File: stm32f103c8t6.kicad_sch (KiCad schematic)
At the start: 0 parts

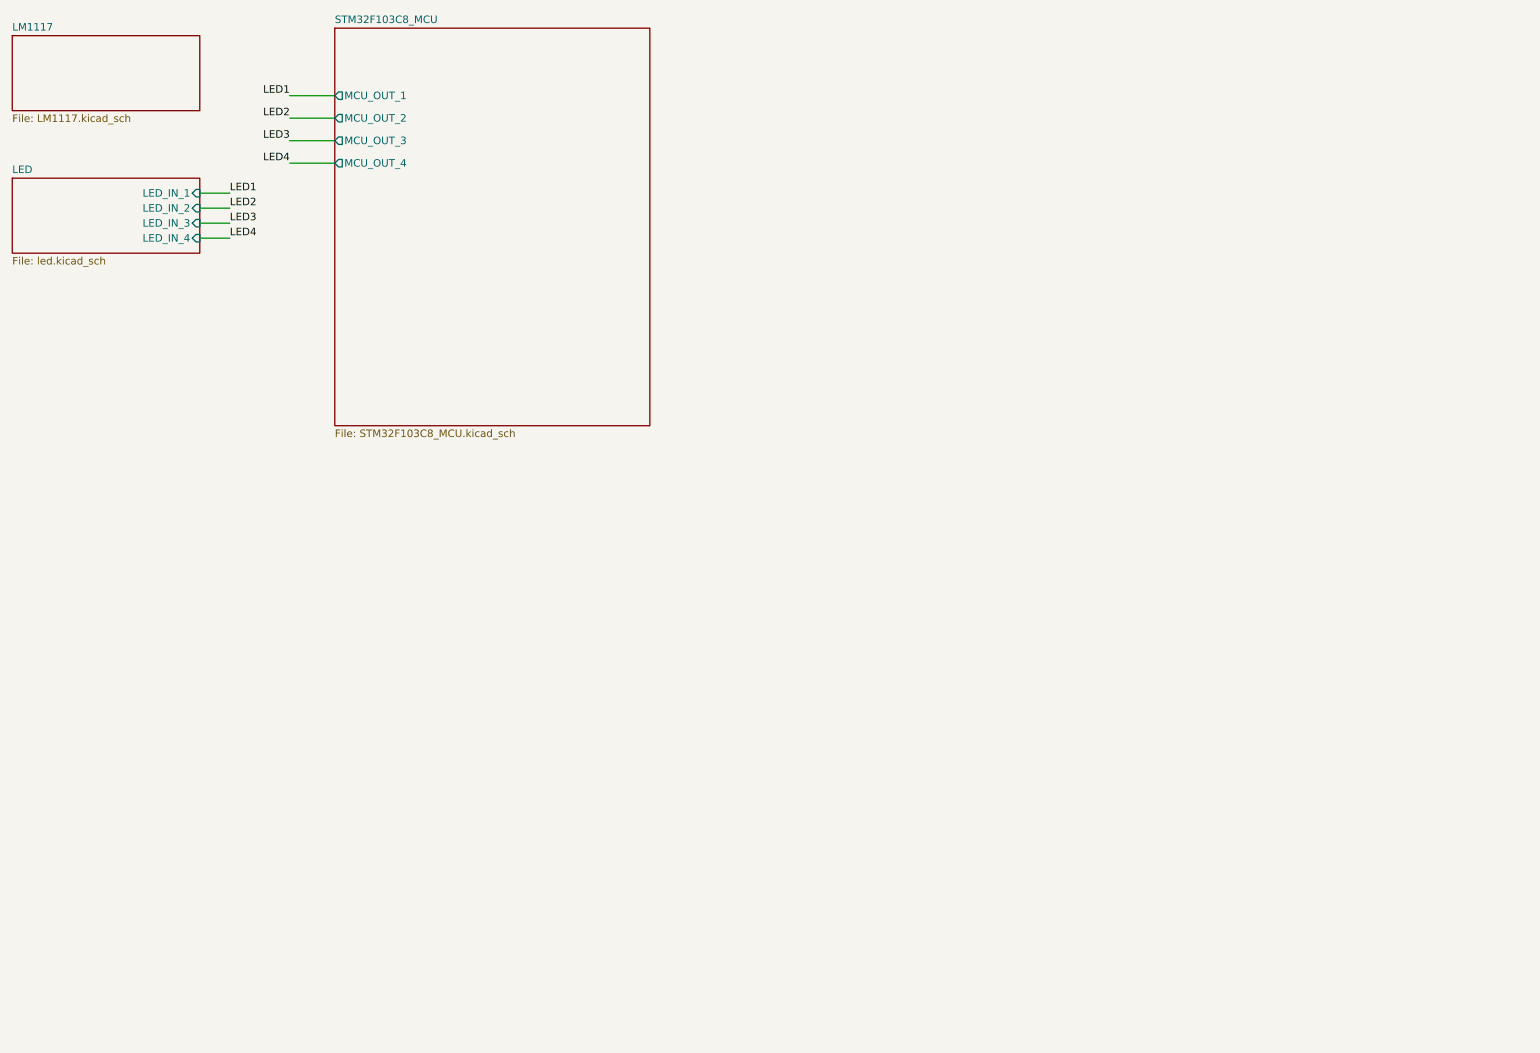
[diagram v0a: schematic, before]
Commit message: Update USB-C and FTDI circuits and add button and potentiometer sheets
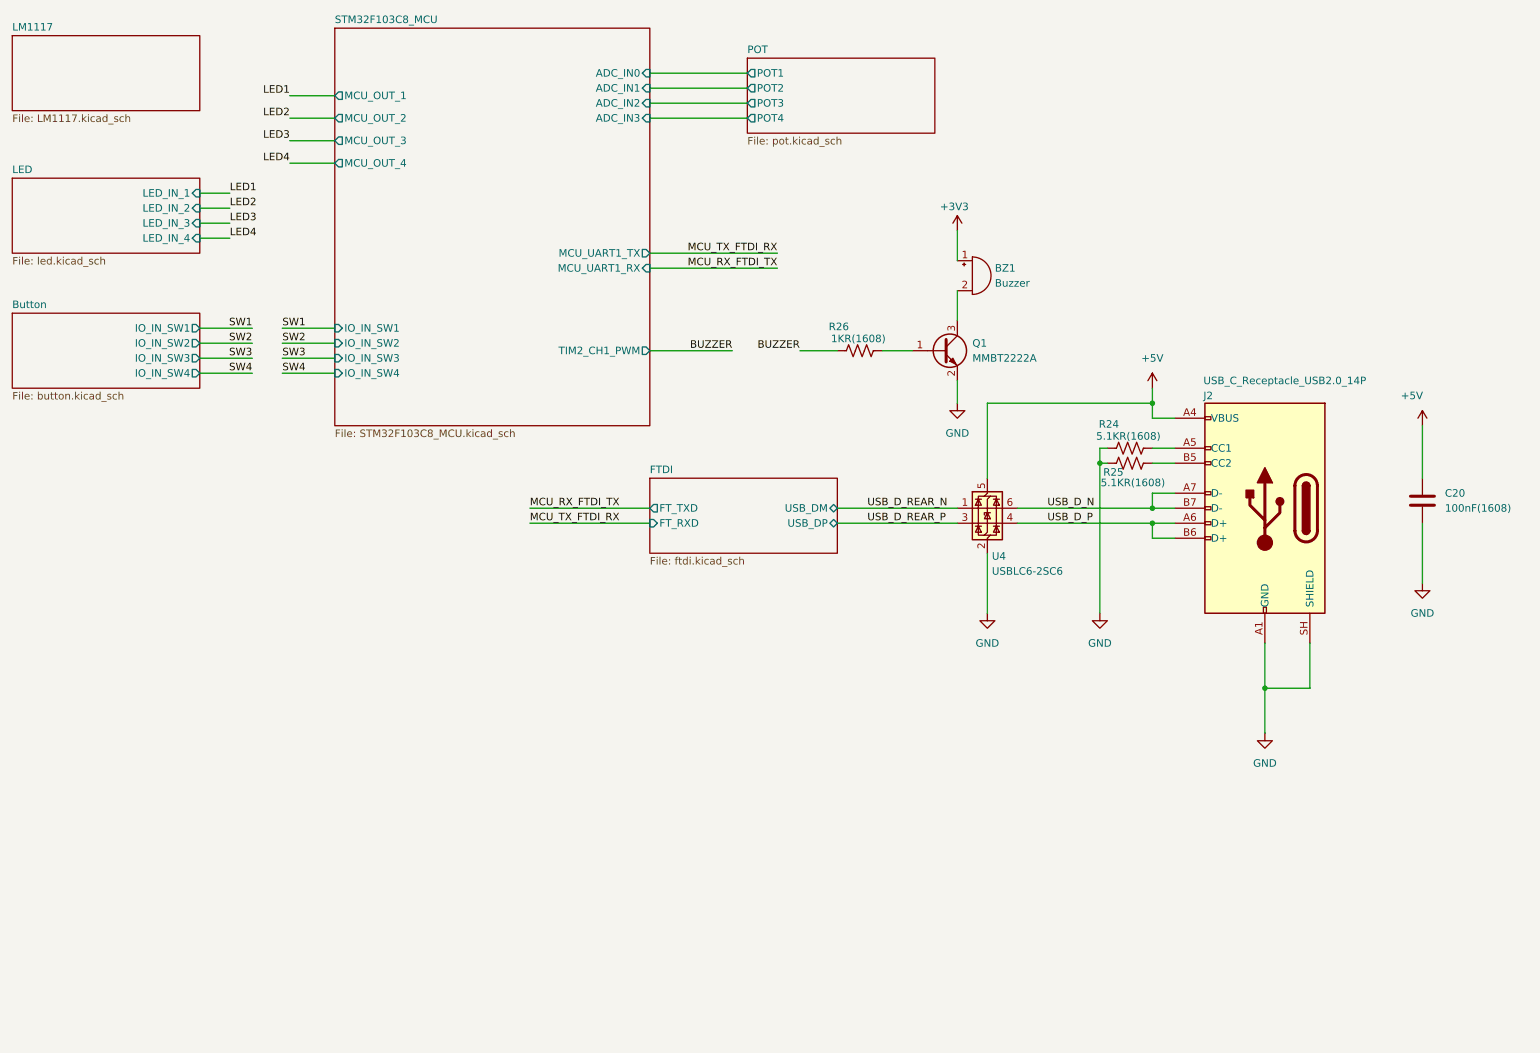
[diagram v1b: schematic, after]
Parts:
- added BZ1: Buzzer, Package_DFN_QFN:Texas_RVA_VQFN-16-1EP_3.5x3.5mm_P0.5mm_EP2.14x2.14mm_ThermalVias, symbol Device:Buzzer
- added C20: 100nF(1608), Capacitor_SMD:C_0603_1608Metric, symbol Device:C
- added J2: USB_C_Receptacle_USB2.0_14P, symbol Connector:USB_C_Receptacle_USB2.0_14P
- added Q1: MMBT2222A, Package_TO_SOT_SMD:SOT-23, symbol Transistor_BJT:MMBT2222A
- added R24, R25: 5.1KR(1608), symbol Device:R_US
- added R26: 1KR(1608), symbol Device:R_US
- added U4: USBLC6-2SC6, Package_TO_SOT_SMD:SOT-23-6, symbol Power_Protection:USBLC6-2SC6
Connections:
- new net: Q1.1 (B), R26.2
- new net: J2.A5 (CC1), R24.2
- new net: BZ1.2 (-), Q1.3 (C)
- new net: J2.B5 (CC2), R25.2
- new net +3V3: BZ1.1 (+)
- new net +5V: C20.1, J2.A4 (VBUS), J2.A9 (VBUS), J2.B4 (VBUS), J2.B9 (VBUS), U4.5 (VBUS)
- new net BUZZER: R26.1
- new net GND: C20.2, J2.A1 (GND), J2.A12 (GND), J2.B1 (GND), J2.B12 (GND), J2.SH (SHIELD), Q1.2 (E), R24.1, R25.1, U4.2 (GND)
- new net USB_D_N: J2.A7 (D-), J2.B7 (D-), U4.6 (I/O1)
- new net USB_D_P: J2.A6 (D+), J2.B6 (D+), U4.4 (I/O2)
- new net USB_D_REAR_N: U4.1 (I/O1)
- new net USB_D_REAR_P: U4.3 (I/O2)
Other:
- added sheet Button (button.kicad_sch)
- added sheet FTDI (ftdi.kicad_sch)
- added sheet POT (pot.kicad_sch)
- sheet STM32F103C8_MCU ports: added ADC_IN0, ADC_IN1, ADC_IN2, ADC_IN3, IO_IN_SW1, IO_IN_SW2, IO_IN_SW3, IO_IN_SW4, MCU_UART1_RX, MCU_UART1_TX, TIM2_CH1_PWM; removed none

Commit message: Update schematics, power flags and PCB design
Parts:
- added H1, H2, H3, H4: MountingHole_Pad, MountingHole:MountingHole_3.2mm_M3_DIN965_Pad, symbol Mechanical:MountingHole_Pad
- added J1: Conn_01x04, Connector_PinHeader_2.54mm:PinHeader_1x04_P2.54mm_Vertical, symbol Connector_Generic:Conn_01x04
- added R1, R2, R3, R4: 0R(1608), Resistor_SMD:R_0603_1608Metric, symbol Device:R_US
- BZ1: footprint Package_DFN_QFN:Texas_RVA_VQFN-16-1EP_3.5x3.5mm_P0.5mm_EP2.14x2.14mm_ThermalVias -> (none)
- R5: renamed from R26; footprint (none) -> Resistor_SMD:R_0603_1608Metric
- R6: renamed from R24; footprint (none) -> Resistor_SMD:R_0603_1608Metric
- R7: renamed from R25; footprint (none) -> Resistor_SMD:R_0603_1608Metric
- renumbered C20 to C1, U4 to U1
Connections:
- net +3V3: now also J1.1 (Pin_1)
- net GND: now also J1.4 (Pin_4), R1.2, R2.2, R3.2, R4.2
- new net: H4.1, R4.1
- new net: H2.1, R2.1
- new net: H1.1, R1.1
- new net: H3.1, R3.1
- new net STM32F103C8_MCU/MCU_UART3_RX: J1.3 (Pin_3)
- new net STM32F103C8_MCU/MCU_UART3_TX: J1.2 (Pin_2)
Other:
- sheet STM32F103C8_MCU ports: added MCU_UART3_RX, MCU_UART3_TX; removed none
- moved on the sheet: BZ1, Q1, R5
